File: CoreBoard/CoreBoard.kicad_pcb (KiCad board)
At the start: 2 copper layers, 144.8 x 89.5 mm, 84 parts, among them J1 RJ45_LED_Shielded, SW1 SW_Push, SW10 SW_Push, SW11 SW_Wuerth_450301014042, SW12 SW_Wuerth_450301014042, SW13 SW_Wuerth_450301014042, SW14 SW_Wuerth_450301014042, SW15 SW_Wuerth_450301014042, SW16 SW_Wuerth_450301014042, SW17 SW_Wuerth_450301014042, SW2 SW_Push, SW3 SW_Push, SW4 SW_Push, SW5 SW_Push, SW6 SW_Push, SW7 SW_Push, SW8 SW_Push, SW9 SW_Push, U1 OKI, U2 Teensy4.1_DEV-16771, U3 SHHD003A0A, U4 GY-521, U5 ATA6561, U6 74HC148, U7 74HC148, U8 74HC00

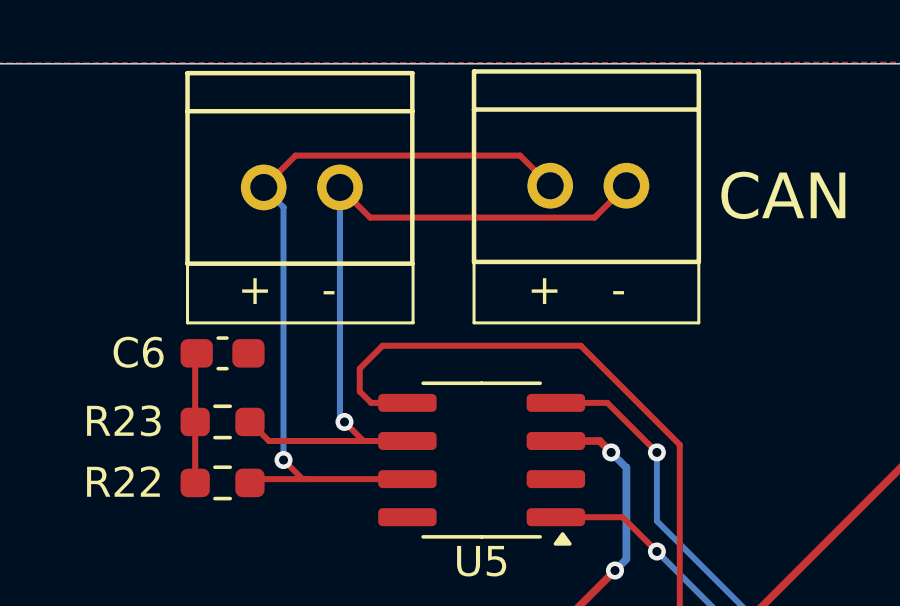
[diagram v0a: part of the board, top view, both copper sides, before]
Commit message: Changed silkscreen for CAN SLs from "+" and "-" to "H" and "L"
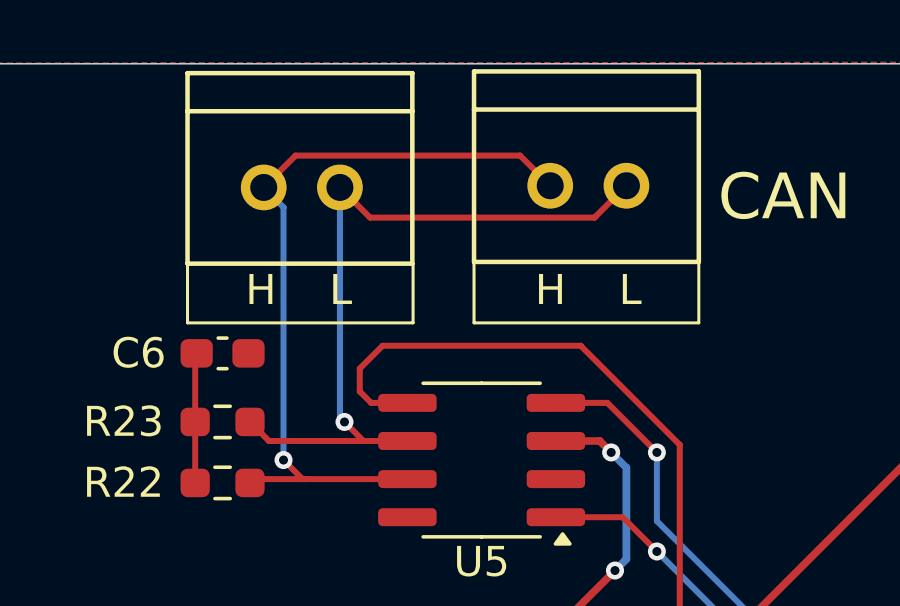
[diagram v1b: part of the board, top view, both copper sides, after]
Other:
- board text added: "H"
- board text added: "L"
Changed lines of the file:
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@@
 		)
 	)
-	(gr_text "+"
-		(at 80.518 46.228 0)
+	(gr_text "H"
+		(at 80.772 46.228 0)
 		(layer "F.SilkS")
 		(effects
@@
 		)
 	)
-	(gr_text "-\n"
-		(at 92.964 46.228 0)
+	(gr_text "L"
+		(at 93.218 46.228 0)
 		(layer "F.SilkS")
 		(effects
@@
 		)
 	)
-	(gr_text "+"
-		(at 90.17 46.228 0)
+	(gr_text "H"
+		(at 90.424 46.228 0)
 		(layer "F.SilkS")
 		(effects
@@
 		)
 	)
-	(gr_text "-\n"
-		(at 83.312 46.228 0)
-		(layer "F.SilkS")
-		(effects
+	(gr_text "L"
+		(at 83.566 46.228 0)
+		(layer "F.SilkS")
+		(effects

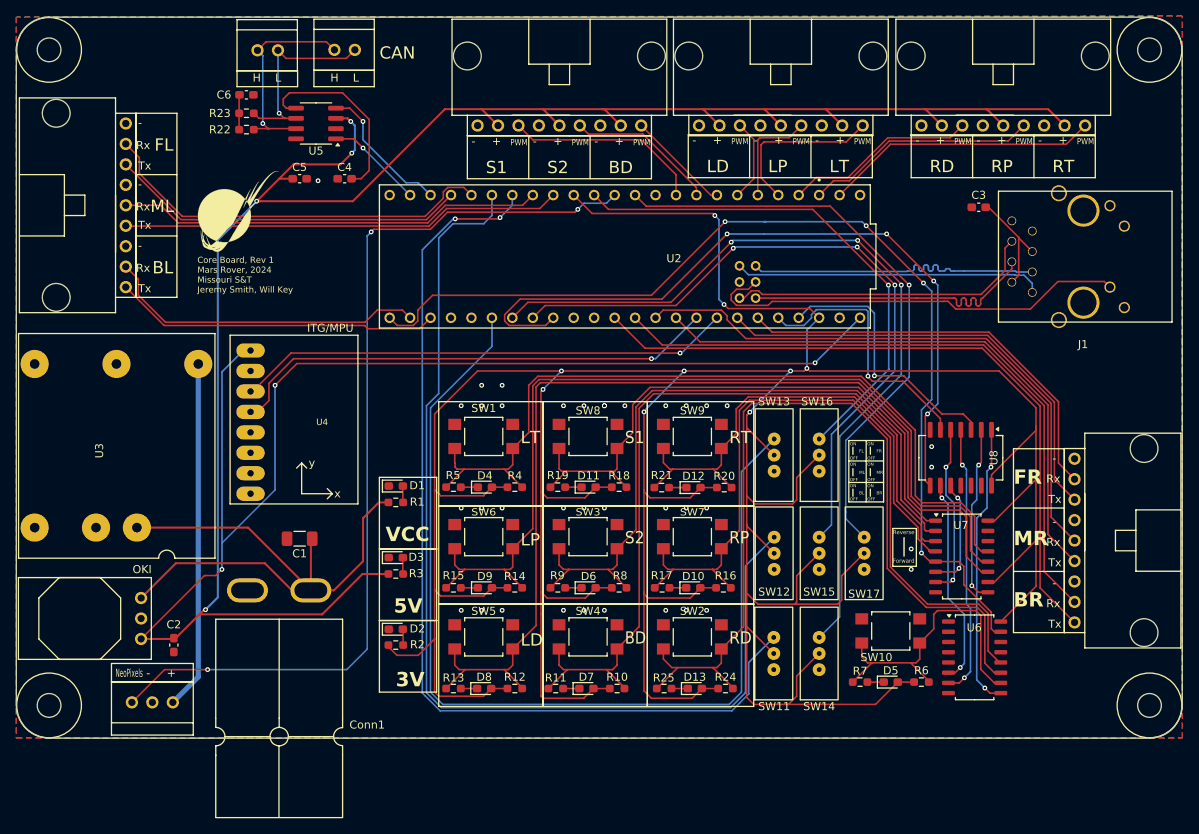
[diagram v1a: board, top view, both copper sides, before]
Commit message: Rearranged CAN layout and merged traces near the Anderson
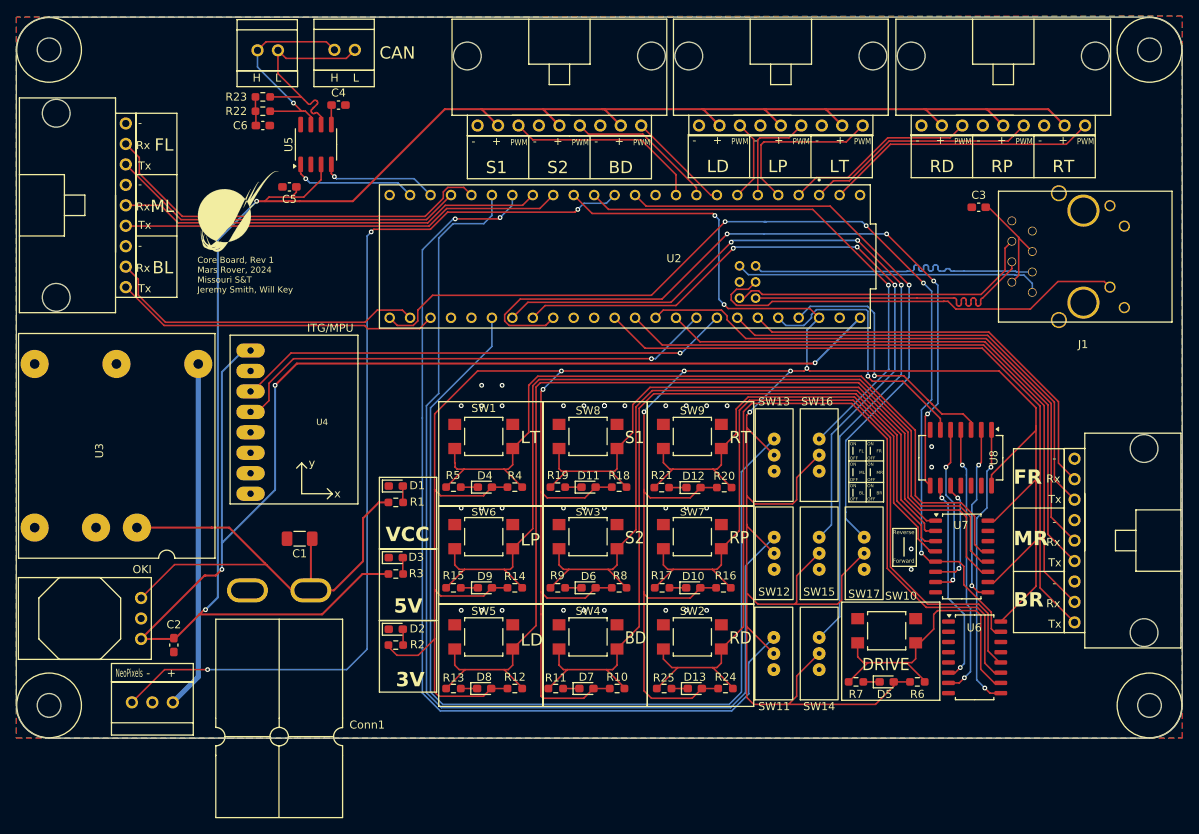
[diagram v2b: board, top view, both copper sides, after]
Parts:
- moved C4 9.18 mm to (91.4, 49.0), turned to 180 degrees
- moved C6 4.32 mm to (82.0, 51.6)
- moved R22 3.06 mm to (82.0, 49.8)
- moved R23 2.87 mm to (82.0, 48.0)
- moved U5 2.60 mm to (88.6, 53.9), turned to 90 degrees
- moved C5 1.63 mm to (85.3, 59.2), turned to 180 degrees
- moved D5 0.51 mm to (159.5, 120.7)
- moved R6 0.51 mm to (163.3, 120.7)
- moved R7 0.51 mm to (155.7, 120.7)
- moved SW10 0.51 mm to (159.5, 114.3)
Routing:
- net +3V3: track 23.8 -> 2.43 mm
- net +5V: track 382.1 -> 370.8 mm, vias 7 -> 5
- net VCC: track 72.9 -> 66.0 mm
- net CAN_TX: track 12.1 -> 15.8 mm
- net CANL: track 24.8 -> 28.0 mm, vias 1 -> 0
- net CAN_RX: track 17.6 -> 14.6 mm
- net Net-(C6-Pad1): track 4.34 -> 3.58 mm
- net GND: vias 37 -> 36
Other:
- board text added: "DRIVE"
